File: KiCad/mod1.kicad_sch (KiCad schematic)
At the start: 63 parts, among them M1 Fan_4pin, M2 Fan_4pin

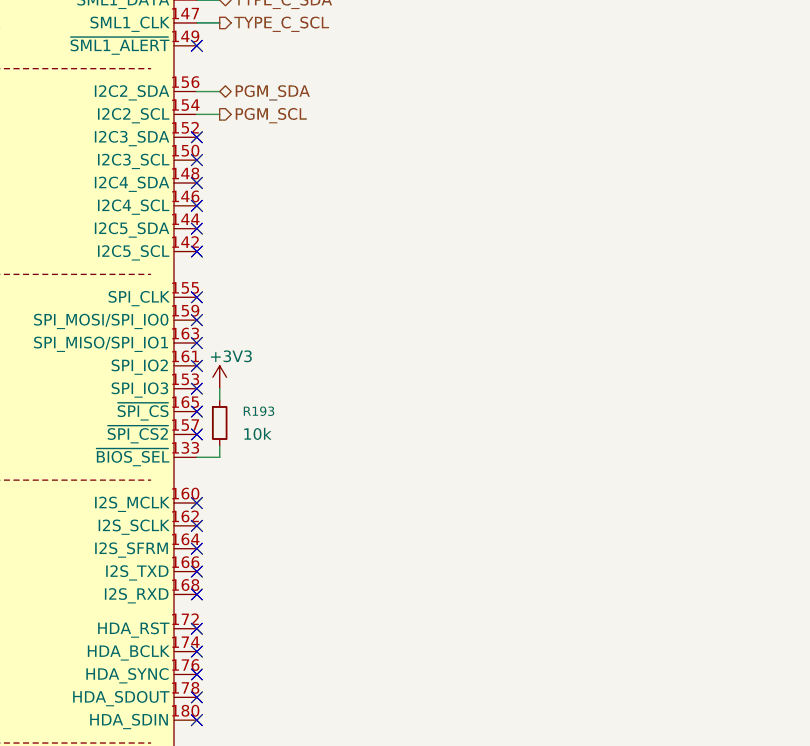
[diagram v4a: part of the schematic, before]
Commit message: Add external BIOS flash
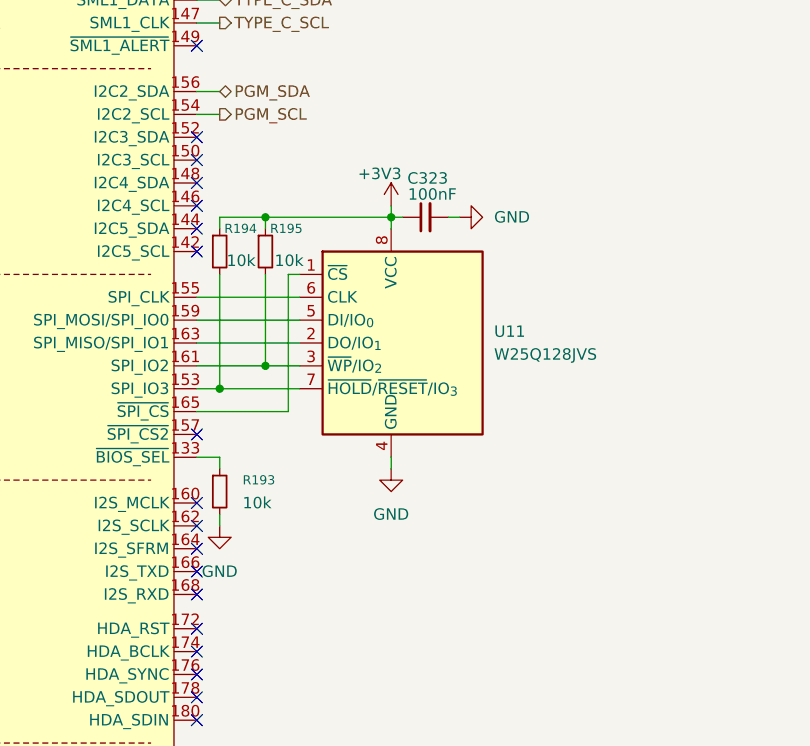
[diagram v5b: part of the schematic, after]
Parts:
- added C323: 100nF, symbol Device:C_Small
- added R194, R195: 10k, symbol Device:R_Small
- added U11: W25Q128JVS, Package_SO:SOIC-8_5.3x5.3mm_P1.27mm, symbol Memory_Flash:W25Q128JVS
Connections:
- net +3V3: now also C323.1, R194.1, R195.1, U11.8 (VCC); no longer R193.1
- net GND: now also R193.2, C323.2, U11.4 (GND)
- net at A1.133 (~{BIOS_SEL}): now also R193.1; no longer R193.2
- net at A1.153 (SPI_IO3): now also R194.2, U11.7 (~{HOLD}/~{RESET}/IO_{3})
- net at A1.155 (SPI_CLK): now also U11.6 (CLK)
- net at A1.159 (SPI_MOSI/SPI_IO0): now also U11.5 (DI/IO_{0})
- net at A1.161 (SPI_IO2): now also R195.2, U11.3 (~{WP}/IO_{2})
- net at A1.163 (SPI_MISO/SPI_IO1): now also U11.2 (DO/IO_{1})
- net at A1.165 (~{SPI_CS}): now also U11.1 (~{CS})
- no-connect marks 87 -> 81
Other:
- moved on the sheet: R193

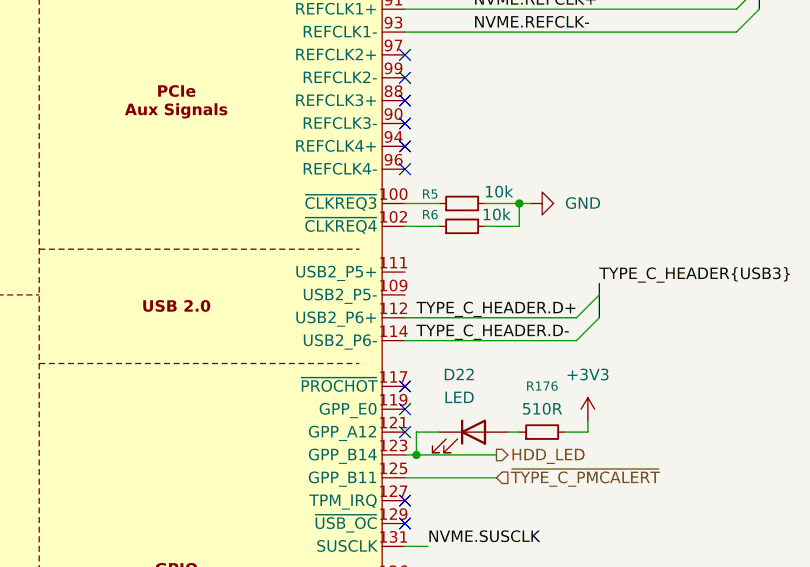
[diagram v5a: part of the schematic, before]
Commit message: Remove 0.95V Power Supply, Replace 3.3V Standby Power Supply
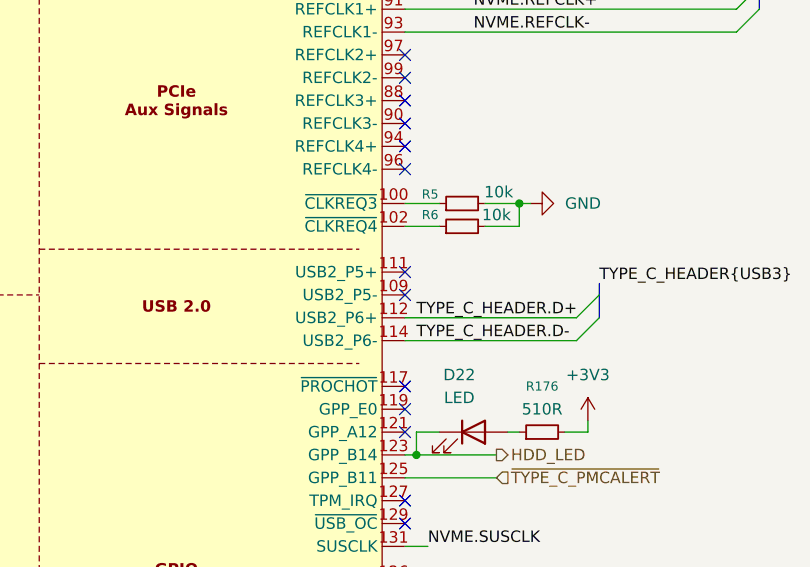
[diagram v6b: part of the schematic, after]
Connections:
- no-connect marks 81 -> 83
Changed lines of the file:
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@@
+	)
+	(no_connect
+		(at 325.12 138.43)
 	)
 	(no_connect
@@
 	)
 	(no_connect
+		(at 325.12 135.89)
+	)
+	(no_connect

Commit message: Work though ERC errors
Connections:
- net ETH.SMBCLK: now reaches A1.106 (SMB_CLK)
- net ETH.SMBDAT: now reaches A1.108 (SMB_DATA)
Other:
- moved on the sheet: R4
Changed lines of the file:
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@@
 	)
 	(junction
+		(at 287.02 72.39)
+		(diameter 0)
+		(color 0 0 0 0)
+	)
+	(junction
 		(at 360.68 41.91)
 		(diameter 0)
@@
 	)
 	(no_connect
-		(at 325.12 217.17)
-	)
-	(no_connect
 		(at 325.12 297.18)
 	)
@@
 	)
 	(no_connect
+		(at 243.84 237.49)
+	)
+	(no_connect
 		(at 325.12 163.83)
 	)
@@
 	)
 	(no_connect
+		(at 243.84 240.03)
+	)
+	(no_connect
 		(at 243.84 295.91)
 	)
@@
 	)
 	(no_connect
-		(at 325.12 214.63)
-	)
-	(no_connect
 		(at 325.12 250.19)
 	)
@@
 	)
 	(bus_entry
+		(at 341.63 212.09)
+		(size -2.54 2.54)
+		(stroke
+			(width 0)
+			(type default)
+		)
+	)
+	(bus_entry
 		(at 217.17 247.65)
 		(size 2.54 2.54)
@@
 	)
 	(bus_entry
+		(at 341.63 214.63)
+		(size -2.54 2.54)
+		(stroke
+			(width 0)
+			(type default)
+		)
+	)
+	(bus_entry
 		(at 217.17 245.11)
 		(size 2.54 2.54)
@@
 		)
 	)
+	(bus
+		(pts
+			(xy 341.63 212.09) (xy 341.63 214.63)
+		)
+		(stroke
+			(width 0)
+			(type default)
+		)
+	)
 	(wire
 		(pts
@@
 	(wire
 		(pts
+			(xy 325.12 214.63) (xy 339.09 214.63)
+		)
+		(stroke
+			(width 0)
+			(type default)
+		)
+	)
+	(wire
+		(pts
 			(xy 214.63 156.21) (xy 243.84 156.21)
 		)
@@
 	(wire
 		(pts
+			(xy 325.12 217.17) (xy 339.09 217.17)
+		)
+		(stroke
+			(width 0)
+			(type default)
+		)
+	)
+	(wire
+		(pts
 			(xy 392.43 57.15) (xy 407.67 57.15)
 		)
@@
 	(wire
 		(pts
-			(xy 287.02 64.77) (xy 287.02 67.31)
+			(xy 287.02 64.77) (xy 287.02 66.04)
 		)
 		(stroke
@@
 	(wire
 		(pts
+			(xy 293.37 72.39) (xy 287.02 72.39)
+		)
+		(stroke
+			(width 0)
+			(type default)
+		)
+	)
+	(wire
+		(pts
 			(xy 237.49 328.93) (xy 243.84 328.93)
 		)
@@
 	(wire
 		(pts
-			(xy 287.02 72.39) (xy 287.02 74.93)
+			(xy 287.02 71.12) (xy 287.02 72.39)
 		)
 		(stroke
@@
 	(wire
 		(pts
+			(xy 293.37 69.85) (xy 293.37 72.39)
+		)
+		(stroke
+			(width 0)
+			(type default)
+		)
+	)
+	(wire
+		(pts
 			(xy 219.71 255.27) (xy 243.84 255.27)
 		)
@@
 	(wire
 		(pts
+			(xy 287.02 72.39) (xy 287.02 74.93)
+		)
+		(stroke
+			(width 0)
+			(type default)
+		)
+	)
+	(wire
+		(pts
 			(xy 334.01 130.81) (xy 337.82 130.81)
 		)
@@
 	(bus
 		(pts
+			(xy 342.9 214.63) (xy 341.63 214.63)
+		)
+		(stroke
+			(width 0)
+			(type default)
+		)
+	)
+	(bus
+		(pts
 			(xy 203.2 157.48) (xy 212.09 157.48)
 		)
@@
 		)
 	)
+	(label "ETH.SMBDAT"
+		(at 326.39 214.63 0)
+		(effects
+			(font
+				(size 1.27 1.27)
+			)
+			(justify left bottom)
+		)
+	)
 	(label "SATA1.Tx-"
 		(at 214.63 163.83 0)
@@
 		)
 	)
+	(label "ETH.SMBCLK"
+		(at 326.39 217.17 0)
+		(effects
+			(font
+				(size 1.27 1.27)
+			)
+			(justify left bottom)
+		)
+	)
 	(label "TYPE_C_HEADER.SS_Tx2+"
 		(at 205.74 323.85 0)
@@
 		)
 	)
+	(label "ETH{PCIE}"
+		(at 342.9 214.63 0)
+		(effects
+			(font
+				(size 1.27 1.27)
+			)
+			(justify left bottom)
+		)
+	)
 	(label "REAR_DISPLAY.HPD"
 		(at 220.98 227.33 0)
@@
 	(symbol
 		(lib_id "Device:R_Small")
-		(at 287.02 69.85 0)
+		(at 287.02 68.58 0)
 		(unit 1)
 		(exclude_from_sim no)
@@
 		(fields_autoplaced yes)
 		(property "Reference" "R4"
-			(at 289.56 68.5799 0)
+			(at 289.56 67.3099 0)
 			(effects
 				(font
@@
 		)
 		(property "Value" "1k"
-			(at 289.56 71.1199 0)
+			(at 289.56 69.8499 0)
 			(effects
 				(font
@@
 		)
 		(property "Footprint" ""
-			(at 287.02 69.85 0)
+			(at 287.02 68.58 0)
 			(effects
 				(font
@@
 		)
 		(property "Datasheet" "~"
-			(at 287.02 69.85 0)
+			(at 287.02 68.58 0)
 			(effects
 				(font
@@
 		)
 		(property "Description" "Resistor, small symbol"
-			(at 287.02 69.85 0)
+			(at 287.02 68.58 0)
 			(effects
 				(font
@@
 					(unit 1)
 				)
+			)
+		)
+	)
+	(symbol
+		(lib_id "power:PWR_FLAG")
+		(at 293.37 69.85 0)
+		(unit 1)
+		(exclude_from_sim no)
+		(in_bom yes)
+		(on_board yes)
+		(dnp no)
+		(fields_autoplaced yes)
+		(property "Reference" "#FLG011"
+			(at 293.37 67.945 0)
+			(effects
+				(font
+					(size 1.27 1.27)
+				)
+				(hide yes)
+			)
+		)
+		(property "Value" "PWR_FLAG"
+			(at 293.37 64.77 0)
+			(effects
+				(font
+					(size 1.27 1.27)
+				)
+			)
+		)
+		(property "Footprint" ""
+			(at 293.37 69.85 0)
+			(effects
+				(font
+					(size 1.27 1.27)
+				)
+				(hide yes)
+			)
+		)
+		(property "Datasheet" "~"
+			(at 293.37 69.85 0)
+			(effects
+				(font
+					(size 1.27 1.27)
+				)
+				(hide yes)
+			)
+		)
+		(property "Description" "Special symbol for telling ERC where power comes from"
+			(at 293.37 69.85 0)
+			(effects
+				(font
+					(size 1.27 1.27)
+				)
+				(hide yes)
+			)
+		)
+		(pin "1"
+		)
+		(instances
+			(project ""
+				(path "/49abeb3a-c598-45a3-ba6b-595eb04f17a8/cc93c412-65e2-4480-b680-2bef174a6ac7"
+					(reference "#FLG011")
+					(unit 1)
+				)

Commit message: Re-annotate components
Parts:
- C19, C20: value 100nF -> 220nF
- renumbered C115 to C31, C323 to C32, C116 to C33, D17 to D1, D22 to D2, D7 to D3, D8 to D4, R163 to R1, R5 to R10, R6 to R11, R170 to R12, R171 to R13, R172 to R14, R173 to R15, R174 to R16, R175 to R17, R195 to R18, R129 to R19, R1 to R2, R130 to R20, R176 to R21, R128 to R22, R132 to R23, R133 to R24, R134 to R25, R135 to R26, R2 to R3, R3 to R4, R168 to R5, R169 to R6, R4 to R7, R194 to R8, R193 to R9, U11 to U1
